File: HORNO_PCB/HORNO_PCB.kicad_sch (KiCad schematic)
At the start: 171 parts, among them J0_10 Terminales de tornillo espaci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, J0_13 Terminales de tornillo espaci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, J0_14 Terminales de tornillo espaci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, J0_18 Terminales de tornillo espaci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, J0_3 Terminales de tornillo espaci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, J0_4 Terminales de tornillo espaci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, J0_5 Terminales de tornillo espaci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, J0_6 Terminales de tornillo espaci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, J0_7 Terminales de tornillo espaci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, J0_8 Terminales de tornillo espaci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, J0_9 Terminales de tornillo espaci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, J1 switch, J2 switch, J3 switch, J4 switch, J5 switch, J6 switch, J7 24VDC, K1 Relay 1, K2 Relay 2, K6 Relay 4, K7 Relay 3, K8 Relay 2, K9 Relay 1, Q1 2N2222, Q2 2N2222, Q6 IRG4PF50W, Q7 IRG4PF50W, U1 TLP521-1, U10 LM741, U15 TLP250, U17 LM741, U18 LM741, U19 TLP250, U2 TLP521-1, U25 UDN2981A, U3 TLP521-1, U4 TLP521-1, U9 LM741

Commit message: Actualizacion de esquematico
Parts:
- removed PX45, PX55, PX62, PX69, PX73, PX74, PX75, PX76, PX77, PX78, PX79, PX81, PX82, PX83, PX84, PX85: ~, Connector_Wire:SolderWire-0.75sqmm_1x01_D1.25mm_OD2.3mm, symbol Connector:Screw_Terminal_01x01
- removed R29, R30, R31: 2.2 KΩ - 1/4 W, Resistor_THT:R_Axial_DIN0309_L9.0mm_D3.2mm_P15.24mm_Horizontal, symbol Device:R_US
- added F1: Fuse, Fuse:Fuseholder_Cylinder-5x20mm_Schurter_0031_8201_Horizontal_Open, symbol Device:Fuse
- added J10, J11, J12, J13, J14, J15, J16, J17, J18, J19, J20, J21, J22, J23, J8, J9: switch, TerminalBlock_MetzConnect:TerminalBlock_MetzConnect_360271_1x01_Horizontal_ScrewM3.0_Boxed, symbol Connector:Screw_Terminal_01x01
- added R12, R7, R8: 2.4 KΩ - 1/2 W, Resistor_THT:R_Axial_DIN0309_L9.0mm_D3.2mm_P15.24mm_Horizontal, symbol Device:R_US
- 3V3a, 3V3b, 5Va, 5Vb, CS1, CS2, CS3, GND1, GND2, GND3, GND4, GND5, GND6, IN1NEG, IN1POS, IN2NEG, IN2POS, IN3NEG, IN3POS, NC1, NC10, NC11, NC12, NC13, NC14, NC15, NC2, NC3, NC4, NC5, NC6, NC7, NC8, NC9, P0, P12, P13, P14, P15, P16, P17, P18, P19, P2, P21, P22, P23, P25, P26, P27, P32, P33, P34, P35, P36, P37, P38, P39, P4, P5, RST, RX, SCK1, SCK2, SCK3, SO1, SO2, SO3, TX, VCC1, VCC2, VCC3: footprint Connector_Wire:SolderWire-0.75sqmm_1x01_D1.25mm_OD2.3mm -> TerminalBlock_MetzConnect:TerminalBlock_MetzConnect_360271_1x01_Horizontal_ScrewM3.0_Boxed
- J0_10, J0_13, J0_14, J0_18, J0_3, J0_4, J0_5, J0_6, J0_7, J0_8, J0_9: value Terminales de tornillo espaciados en 3.5mm -> Terminales de tornillo espaciados en 5mm; footprint TerminalBlock_Phoenix:TerminalBlock_Phoenix_PT-1,5-3-3.5-H_1x03_P3.50mm_Horizontal -> TerminalBlock_Phoenix:TerminalBlock_Phoenix_PT-1,5-3-5.0-H_1x03_P5.00mm_Horizontal
- J1, J2, J3, J4, J5, J6: footprint (none) -> TerminalBlock_MetzConnect:TerminalBlock_MetzConnect_360271_1x01_Horizontal_ScrewM3.0_Boxed
- J7: footprint (none) -> TerminalBlock_Phoenix:TerminalBlock_Phoenix_PT-1,5-3-5.0-H_1x03_P5.00mm_Horizontal
- K1, K2, K6, K7, K8, K9: footprint Relay_THT:Relay_SPDT_SANYOU_SRD_Series_Form_C -> Relay_THT:Relay_SPDT_Fujitsu_FTR-LYCA005x_FormC_Vertical
- Q6, Q7: footprint Package_TO_SOT_THT:TO-264-3_Vertical -> Package_TO_SOT_THT:TO-247-3_Vertical
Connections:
- net at D3.2 (A): now also R8.2
- net at 5Va.1 (Pin_1), 5Vb.1 (Pin_1), R1.2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: now also J11.1 (Pin_1), J21.1 (Pin_1); no longer J0_14.3 (Pin_3), J0_18.3 (Pin_3), Q6.3 (E), Q7.3 (E)
- net at C10.2, C5.2, C6.2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: now also J0_14.3 (Pin_3), J0_18.3 (Pin_3), Q6.3 (E), Q7.3 (E), J10.1 (Pin_1), J12.1 (Pin_1), J15.1 (Pin_1), J16.1 (Pin_1), J18.1 (Pin_1), J20.1 (Pin_1), J22.1 (Pin_1), J9.1 (Pin_1); no longer U15.5 (VEE), U19.5 (VEE)
- net at U10.4 (V-), U17.4 (V-), U18.4 (V-)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: now also U15.5 (VEE), U19.5 (VEE), J14.1 (Pin_1)
- net at U10.7 (V+), U15.8 (VCC), U17.7 (V+)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: now also U25.9 (Vs), J8.1 (Pin_1)
- net at D10.2 (A), D11.2 (A), D12.2 (A)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: now also F1.1, J17.1 (Pin_1), J23.1 (Pin_1), R12.1; no longer J7.1 (Pin_1), U25.9 (Vs)
- net at J0_10.1 (Pin_1): now also K6.3; no longer K6.1
- net at J0_10.2 (Pin_2): now also K6.1; no longer K6.3
- net at D4.2 (A): now also R12.2
- net at K1.1: now also J0_4.2 (Pin_2); no longer J0_4.1 (Pin_1)
- net at K1.3: now also J0_4.1 (Pin_1); no longer J0_4.2 (Pin_2)
- net at J3.1 (Pin_1): now also R7.1
- net at D2.2 (A): now also R7.2
- net at CS1.1 (Pin_1), CS2.1 (Pin_1), CS3.1 (Pin_1)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: now also J13.1 (Pin_1)
- net at J5.1 (Pin_1): now also R8.1
- net at J0_9.1 (Pin_1): now also K7.3; no longer K7.1
- net at J0_9.2 (Pin_2): now also K7.1; no longer K7.3
- net at K2.1: now also J0_6.2 (Pin_2); no longer J0_6.1 (Pin_1)
- net at K2.3: now also J0_6.1 (Pin_1); no longer J0_6.2 (Pin_2)
- net at K9.1: now also J0_7.2 (Pin_2); no longer J0_7.1 (Pin_1)
- net at K9.3: now also J0_7.1 (Pin_1); no longer J0_7.2 (Pin_2)
- net at J0_8.1 (Pin_1): now also K8.3; no longer K8.1
- net at J0_8.2 (Pin_2): now also K8.1; no longer K8.3
- new net: F1.2, J7.1 (Pin_1)
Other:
- note removed: "-5 voltios"
- moved on the sheet: J7

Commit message: Actualizacion de PCB
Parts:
- added J24: Screw_Terminal_01x20, Connector_PinHeader_2.54mm:PinHeader_1x20_P2.54mm_Vertical, symbol Connector:Screw_Terminal_01x20
- renumbered 3V3a to 3V3a1, 3V3b to 3V3b1, 5Va to 5Va1, 5Vb to 5Vb1, IN1NEG to IN1NEG1, IN1POS to IN1POS1, IN2NEG to IN2NEG1, IN2POS to IN2POS1, IN3NEG to IN3NEG1, IN3POS to IN3POS1, RST to RST1, RX to RX1, TX to TX1
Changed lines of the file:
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@@
 		(on_board yes)
 		(dnp no)
-		(property "Reference" "IN3POS"
+		(property "Reference" "IN3POS1"
 			(at 643.636 286.004 0)
 			(effects
@@
 			(project "HORNO_PCB"
 				(path "/70384b34-09dd-4fe3-975b-9645e85de3d4"
-					(reference "IN3POS")
+					(reference "IN3POS1")
 					(unit 1)
 				)
@@
 		(on_board yes)
 		(dnp no)
-		(property "Reference" "RST"
+		(property "Reference" "RST1"
 			(at 600.964 162.56 0)
 			(effects
@@
 			(project "HORNO_PCB"
 				(path "/70384b34-09dd-4fe3-975b-9645e85de3d4"
-					(reference "RST")
+					(reference "RST1")
 					(unit 1)
 				)
@@
 		(on_board yes)
 		(dnp no)
-		(property "Reference" "5Vb"
+		(property "Reference" "5Vb1"
 			(at 643.636 149.86 0)
 			(effects
@@
 			(project "HORNO_PCB"
 				(path "/70384b34-09dd-4fe3-975b-9645e85de3d4"
-					(reference "5Vb")
+					(reference "5Vb1")
 					(unit 1)
 				)
@@
 		(on_board yes)
 		(dnp no)
-		(property "Reference" "5Va"
+		(property "Reference" "5Va1"
 			(at 600.964 149.86 0)
 			(effects
@@
 			(project "HORNO_PCB"
 				(path "/70384b34-09dd-4fe3-975b-9645e85de3d4"
-					(reference "5Va")
+					(reference "5Va1")
 					(unit 1)
 				)
@@
 		(on_board yes)
 		(dnp no)
-		(property "Reference" "3V3b"
+		(property "Reference" "3V3b1"
 			(at 643.636 152.4 0)
 			(effects
@@
 			(project "HORNO_PCB"
 				(path "/70384b34-09dd-4fe3-975b-9645e85de3d4"
-					(reference "3V3b")
+					(reference "3V3b1")
 					(unit 1)
 				)
@@
 		(on_board yes)
 		(dnp no)
-		(property "Reference" "IN2NEG"
+		(property "Reference" "IN2NEG1"
 			(at 643.382 275.336 0)
 			(effects
@@
 			(project "HORNO_PCB"
 				(path "/70384b34-09dd-4fe3-975b-9645e85de3d4"
-					(reference "IN2NEG")
+					(reference "IN2NEG1")
 					(unit 1)
 				)
@@
 		(on_board yes)
 		(dnp no)
-		(property "Reference" "IN1POS"
+		(property "Reference" "IN1POS1"
 			(at 643.636 255.27 0)
 			(effects
@@
 			(project "HORNO_PCB"
 				(path "/70384b34-09dd-4fe3-975b-9645e85de3d4"
-					(reference "IN1POS")
+					(reference "IN1POS1")
 					(unit 1)
 				)
@@
 		(on_board yes)
 		(dnp no)
-		(property "Reference" "IN2POS"
+		(property "Reference" "IN2POS1"
 			(at 643.382 270.51 0)
 			(effects
@@
 			(project "HORNO_PCB"
 				(path "/70384b34-09dd-4fe3-975b-9645e85de3d4"
-					(reference "IN2POS")
+					(reference "IN2POS1")
 					(unit 1)
 				)
@@
 		(on_board yes)
 		(dnp no)
-		(property "Reference" "IN1NEG"
+		(property "Reference" "IN1NEG1"
 			(at 643.636 260.35 0)
 			(effects
@@
 			(project "HORNO_PCB"
 				(path "/70384b34-09dd-4fe3-975b-9645e85de3d4"
-					(reference "IN1NEG")
+					(reference "IN1NEG1")
 					(unit 1)
 				)
@@
 		(on_board yes)
 		(dnp no)
-		(property "Reference" "TX"
+		(property "Reference" "TX1"
 			(at 600.71 159.766 0)
 			(effects
@@
 			(project "HORNO_PCB"
 				(path "/70384b34-09dd-4fe3-975b-9645e85de3d4"
-					(reference "TX")
+					(reference "TX1")
 					(unit 1)
 				)
@@
 		(on_board yes)
 		(dnp no)
-		(property "Reference" "IN3NEG"
+		(property "Reference" "IN3NEG1"
 			(at 643.636 290.83 0)
 			(effects
@@
 			(project "HORNO_PCB"
 				(path "/70384b34-09dd-4fe3-975b-9645e85de3d4"
-					(reference "IN3NEG")
+					(reference "IN3NEG1")
 					(unit 1)
 				)
@@
 		(on_board yes)
 		(dnp no)
-		(property "Reference" "3V3a"
+		(property "Reference" "3V3a1"
 			(at 601.472 152.4 0)
 			(effects
@@
 			(project "HORNO_PCB"
 				(path "/70384b34-09dd-4fe3-975b-9645e85de3d4"
-					(reference "3V3a")
+					(reference "3V3a1")
 					(unit 1)
 				)
@@
 	)
 	(symbol
+		(lib_id "Connector:Screw_Terminal_01x20")
+		(at 681.99 93.98 90)
+		(unit 1)
+		(exclude_from_sim no)
+		(in_bom yes)
+		(on_board yes)
+		(dnp no)
+		(fields_autoplaced yes)
+		(property "Reference" "J24"
+			(at 683.26 87.63 90)
+			(effects
+				(font
+					(size 1.27 1.27)
+				)
+			)
+		)
+		(property "Value" "Screw_Terminal_01x20"
+			(at 683.26 90.17 90)
+			(effects
+				(font
+					(size 1.27 1.27)
+				)
+			)
+		)
+		(property "Footprint" "Connector_PinHeader_2.54mm:PinHeader_1x20_P2.54mm_Vertical"
+			(at 681.99 93.98 0)
+			(effects
+				(font
+					(size 1.27 1.27)
+				)
+				(hide yes)
+			)
+		)
+		(property "Datasheet" "~"
+			(at 681.99 93.98 0)
+			(effects
+				(font
+					(size 1.27 1.27)
+				)
+				(hide yes)
+			)
+		)
+		(property "Description" "Generic screw terminal, single row, 01x20, script generated (kicad-library-utils/schlib/autogen/connector/)"
+			(at 681.99 93.98 0)
+			(effects
+				(font
+					(size 1.27 1.27)
+				)
+				(hide yes)
+			)
+		)
+		(pin "17"
+		)
+		(pin "16"
+		)
+		(pin "15"
+		)
+		(pin "10"
+		)
+		(pin "8"
+		)
+		(pin "11"
+		)
+		(pin "20"
+		)
+		(pin "4"
+		)
+		(pin "3"
+		)
+		(pin "12"
+		)
+		(pin "14"
+		)
+		(pin "1"
+		)
+		(pin "13"
+		)
+		(pin "2"
+		)
+		(pin "5"
+		)
+		(pin "18"
+		)
+		(pin "9"
+		)
+		(pin "6"
+		)
+		(pin "7"
+		)
+		(pin "19"
+		)
+		(instances
+			(project "HORNO_PCB"
+				(path "/70384b34-09dd-4fe3-975b-9645e85de3d4"
+					(reference "J24")
+					(unit 1)
+				)
+			)
+		)
+	)
+	(symbol
 		(lib_id "Isolator:Optocoupler_DC_PhotoNPN_AKEC")
 		(at 179.07 335.28 0)
@@
 		(on_board yes)
 		(dnp no)
-		(property "Reference" "RX"
+		(property "Reference" "RX1"
 			(at 600.71 157.48 0)
 			(effects
@@
 			(project "HORNO_PCB"
 				(path "/70384b34-09dd-4fe3-975b-9645e85de3d4"
-					(reference "RX")
+					(reference "RX1")
 					(unit 1)
 				)

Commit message: Organizacion de modulos en PCB
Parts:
- removed 3V3a1, 3V3b1, 5Va1, 5Vb1, CS1, CS2, CS3, GND1, GND2, GND3, GND4, GND5, GND6, IN1NEG1, IN1POS1, IN2NEG1, IN2POS1, IN3NEG1, IN3POS1, NC1, NC10, NC11, NC12, NC13, NC14, NC15, NC2, NC3, NC4, NC5, NC6, NC7, NC8, NC9, P0, P12, P13, P14, P15, P16, P17, P18, P19, P2, P21, P22, P23, P25, P26, P27, P32, P33, P34, P35, P36, P37, P38, P39, P4, P5, RST1, RX1, SCK1, SCK2, SCK3, SO1, SO2, SO3, TX1, VCC1, VCC2, VCC3: ~, TerminalBlock_MetzConnect:TerminalBlock_MetzConnect_360271_1x01_Horizontal_ScrewM3.0_Boxed, symbol Connector:Screw_Terminal_01x01
- added J0_1: Terminales de tornillo espaciados en 5mm, TerminalBlock_Phoenix:TerminalBlock_Phoenix_PT-1,5-3-5.0-H_1x03_P5.00mm_Horizontal, symbol Connector:Screw_Terminal_01x03
- added J25, J26, J27: Screw_Terminal_01x20, Connector_PinHeader_2.54mm:PinHeader_1x20_P2.54mm_Vertical, symbol Connector:Screw_Terminal_01x20
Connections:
- net at R11.2: now also J24.13 (Pin_13)
- net at C10.2, C5.2, C6.2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: now also J25.20 (Pin_20); no longer C7.2, J0_3.3 (Pin_3)
- net at R3.1, U3.4: now also J25.17 (Pin_17)
- net at C7.1: now also J24.3 (Pin_3)
- net at R26.2: now also J24.17 (Pin_17)
- net at J11.1 (Pin_1), J21.1 (Pin_1), R1.2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: now also J24.2 (Pin_2), J0_1.1 (Pin_1), J0_1.2 (Pin_2), J0_1.3 (Pin_3), J25.19 (Pin_19)
- net at Q1.1 (E), R38.1: now also J25.11 (Pin_11)
- net at R44.2: now also J25.5 (Pin_5)
- net at R2.1, U2.4: now also J25.12 (Pin_12)
- net at R20.2: now also J24.18 (Pin_18)
- net at R4.1, U4.4: now also J25.14 (Pin_14)
- net at Q2.1 (E), R37.1: now also J25.10 (Pin_10)
- net at J13.1 (Pin_1), Q1.3 (C), Q2.3 (C): now also J26.11 (Pin_11), J26.17 (Pin_17), J26.5 (Pin_5)
- net at R46.2: now also J25.4 (Pin_4)
- net at R10.2: now also J24.16 (Pin_16)
- net at C9.1, U18.3 (+): now also J25.8 (Pin_8)
- net at R9.2: now also J24.15 (Pin_15)
- net at C10.1: now also J25.18 (Pin_18)
- net at J0_3.1 (Pin_1): now also J24.5 (Pin_5)
- net at J0_3.2 (Pin_2): now also J24.6 (Pin_6)
- net at R1.1, U1.4: now also J25.13 (Pin_13)
- net at C8.1, U17.3 (+): now also J25.9 (Pin_9)
- net at R48.2: now also J25.6 (Pin_6)
- net at J24.1 (Pin_1): now also C7.2, J0_3.3 (Pin_3)
- net at J24.10 (Pin_10): now also J26.15 (Pin_15), J26.3 (Pin_3), J26.9 (Pin_9)
- net at J24.11 (Pin_11): now also J26.14 (Pin_14)
- net at J24.12 (Pin_12): now also J26.1 (Pin_1), J26.13 (Pin_13), J26.7 (Pin_7)
- net at J24.4 (Pin_4): now also J26.10 (Pin_10), J26.16 (Pin_16), J26.4 (Pin_4)
- net at J24.9 (Pin_9): now also J26.8 (Pin_8)
- new net: J25.3 (Pin_3), J26.2 (Pin_2)
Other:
- note added: "GND 5V 3.3V GND RX TX RST P0 P22 P19 P23 P18 P5 P15 P2 P4 P17 P16"
- note added: "GND 5V 3.3V P36 P37 P38 P39 P34 P35 P32 P33 P25 P26 P27 P14 P12 P13 P21"
- note added: "NC IN1POS NC IN1NEG NC NC NC IN2POS NC IN2NEG NC NC NC IN3POS NC IN3NEG NC NC NC NC"
- note added: "SCK1 CS1 SO1 GND VCC NC SCK2 CS2 SO2 GND VCC NC SCK3 CS3 SO3 GND VCC NC NC NC"
- moved on the sheet: C10, C7, J24

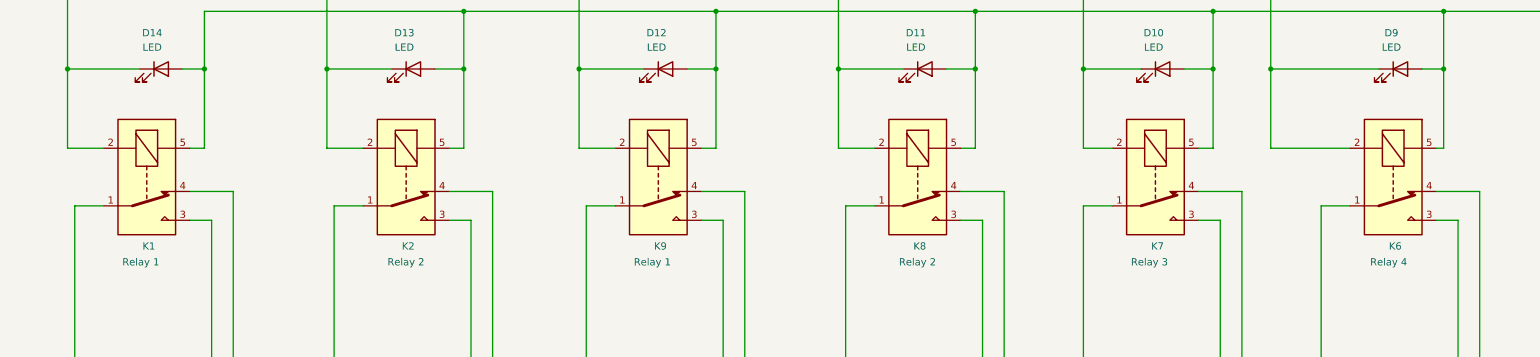
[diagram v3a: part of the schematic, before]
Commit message: Organizacion de modulos en PCB
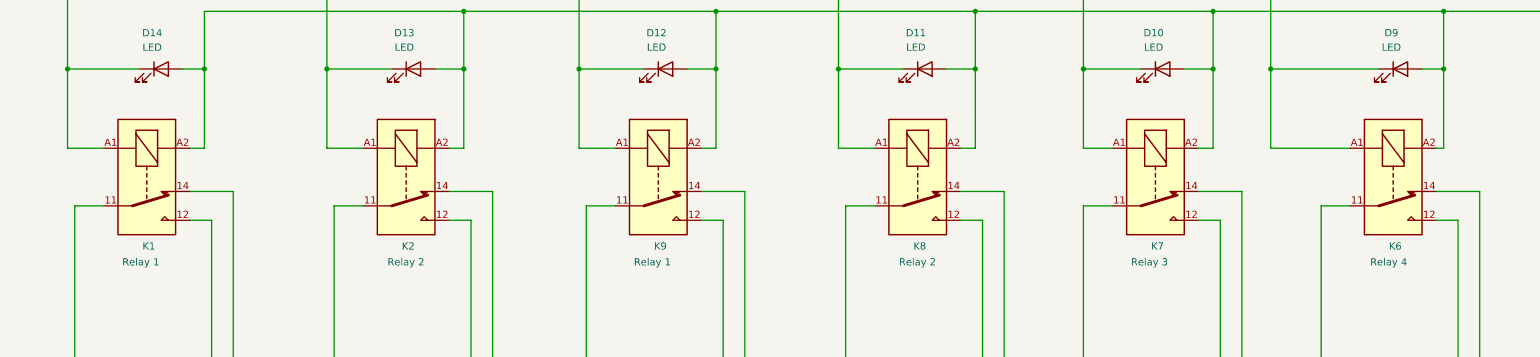
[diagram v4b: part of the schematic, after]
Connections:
- net at D12.1 (K), U25.15 (O4): now also K9.A1; no longer K9.2
- net at D10.2 (A), D11.2 (A), D12.2 (A)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: now also K1.A2, K2.A2, K6.A2, K7.A2, K8.A2, K9.A2; no longer K1.5, K2.5, K6.5, K7.5, K8.5, K9.5
- net at J0_10.1 (Pin_1): now also K6.12; no longer K6.3
- net at J0_10.2 (Pin_2): now also K6.11; no longer K6.1
- net at J0_10.3 (Pin_3): now also K6.14; no longer K6.4
- net at J0_4.2 (Pin_2): now also K1.11; no longer K1.1
- net at D14.1 (K), U25.13 (O6): now also K1.A1; no longer K1.2
- net at J0_4.1 (Pin_1): now also K1.12; no longer K1.3
- net at J0_4.3 (Pin_3): now also K1.14; no longer K1.4
- net at J0_9.1 (Pin_1): now also K7.12; no longer K7.3
- net at J0_9.2 (Pin_2): now also K7.11; no longer K7.1
- net at J0_9.3 (Pin_3): now also K7.14; no longer K7.4
- net at J0_6.2 (Pin_2): now also K2.11; no longer K2.1
- net at D13.1 (K), U25.14 (O5): now also K2.A1; no longer K2.2
- net at J0_6.1 (Pin_1): now also K2.12; no longer K2.3
- net at J0_6.3 (Pin_3): now also K2.14; no longer K2.4
- net at D9.1 (K), U25.18 (O1): now also K6.A1; no longer K6.2
- net at J0_7.2 (Pin_2): now also K9.11; no longer K9.1
- net at J0_7.1 (Pin_1): now also K9.12; no longer K9.3
- net at J0_7.3 (Pin_3): now also K9.14; no longer K9.4
- net at J0_8.1 (Pin_1): now also K8.12; no longer K8.3
- net at J0_8.2 (Pin_2): now also K8.11; no longer K8.1
- net at J0_8.3 (Pin_3): now also K8.14; no longer K8.4
- net at D11.1 (K), U25.16 (O3): now also K8.A1; no longer K8.2
- net at D10.1 (K), U25.17 (O2): now also K7.A1; no longer K7.2
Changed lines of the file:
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@@
 	)
 	(symbol
+		(lib_name "SANYOU_SRD_Form_C_1")
 		(lib_id "Relay:SANYOU_SRD_Form_C")
 		(at 285.75 560.07 270)
@@
 			)
 		)
-		(pin "4"
+		(pin "14"
 		)
-		(pin "5"
+		(pin "A1"
 		)
-		(pin "1"
+		(pin "A2"
 		)
-		(pin "3"
+		(pin "12"
 		)
-		(pin "2"
+		(pin "11"
 		)
 		(instances
@@
 	)
 	(symbol
+		(lib_name "SANYOU_SRD_Form_C_2")
 		(lib_id "Relay:SANYOU_SRD_Form_C")
 		(at 331.47 560.07 270)
@@
 			)
 		)
-		(pin "4"
+		(pin "12"
 		)
-		(pin "5"
+		(pin "A1"
 		)
-		(pin "1"
+		(pin "11"
 		)
-		(pin "3"
+		(pin "14"
 		)
-		(pin "2"
+		(pin "A2"
 		)
 		(instances
@@
 			)
 		)
-		(pin "4"
+		(pin "12"
 		)
-		(pin "5"
+		(pin "14"
 		)
-		(pin "1"
+		(pin "11"
 		)
-		(pin "3"
+		(pin "A1"
 		)
-		(pin "2"
+		(pin "A2"
 		)
 		(instances
@@
 	)
 	(symbol
+		(lib_name "SANYOU_SRD_Form_C_3")
 		(lib_id "Relay:SANYOU_SRD_Form_C")
 		(at 375.92 560.07 270)
@@
 			)
 		)
-		(pin "4"
+		(pin "14"
 		)
-		(pin "5"
+		(pin "12"
 		)
-		(pin "1"
+		(pin "A1"
 		)
-		(pin "3"
+		(pin "A2"
 		)
-		(pin "2"
+		(pin "11"
 		)
 		(instances
@@
 	)
 	(symbol
+		(lib_name "SANYOU_SRD_Form_C_5")
 		(lib_id "Relay:SANYOU_SRD_Form_C")
 		(at 463.55 560.07 270)
@@
 			)
 		)
-		(pin "4"
+		(pin "14"
 		)
-		(pin "5"
+		(pin "A1"
 		)
-		(pin "1"
+		(pin "11"
 		)
-		(pin "3"
+		(pin "A2"
 		)
-		(pin "2"
+		(pin "12"
 		)
 		(instances
@@
 	)
 	(symbol
+		(lib_name "SANYOU_SRD_Form_C_4")
 		(lib_id "Relay:SANYOU_SRD_Form_C")
 		(at 421.64 560.07 270)
@@
 			)
 		)
-		(pin "4"
+		(pin "11"
 		)
-		(pin "5"
+		(pin "A1"
 		)
-		(pin "1"
+		(pin "14"
 		)
-		(pin "3"
+		(pin "12"
 		)
-		(pin "2"
+		(pin "A2"
 		)
 		(instances
